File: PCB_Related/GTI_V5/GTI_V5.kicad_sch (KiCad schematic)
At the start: 165 parts, among them IC3 MAX253CSA+, IC4 AMC1306M25QDWVRQ1, IC5 AMC1306M25QDWVRQ1, IC6 AMC1306M25QDWVRQ1, IC7 MAX253CSA+, IC8 MAX253CSA+, IC9 AMC1306M25QDWVRQ1, J1 Screw_Terminal_01x03, J2 Screw_Terminal_01x02, J3 Screw_Terminal_01x02, J4 Conn_01x05_Male, J5 Conn_01x02_Male, J6 Conn_01x02_Male, K1 G5LE-1, K2 G5LE-1, Q1 BUZ11, Q2 2N7002, Q3 BUZ11, Q4 BUZ11, Q5 BUZ11, T1 760390014, T2 760390014, T3 760390014, U1 STM32L475RCTx, U2 UCC21520ADW, U3 AZ1117-5.0, U4 NCP1117-3.3_SOT223, U5 UCC21520ADW, Y1 Crystal_GND24

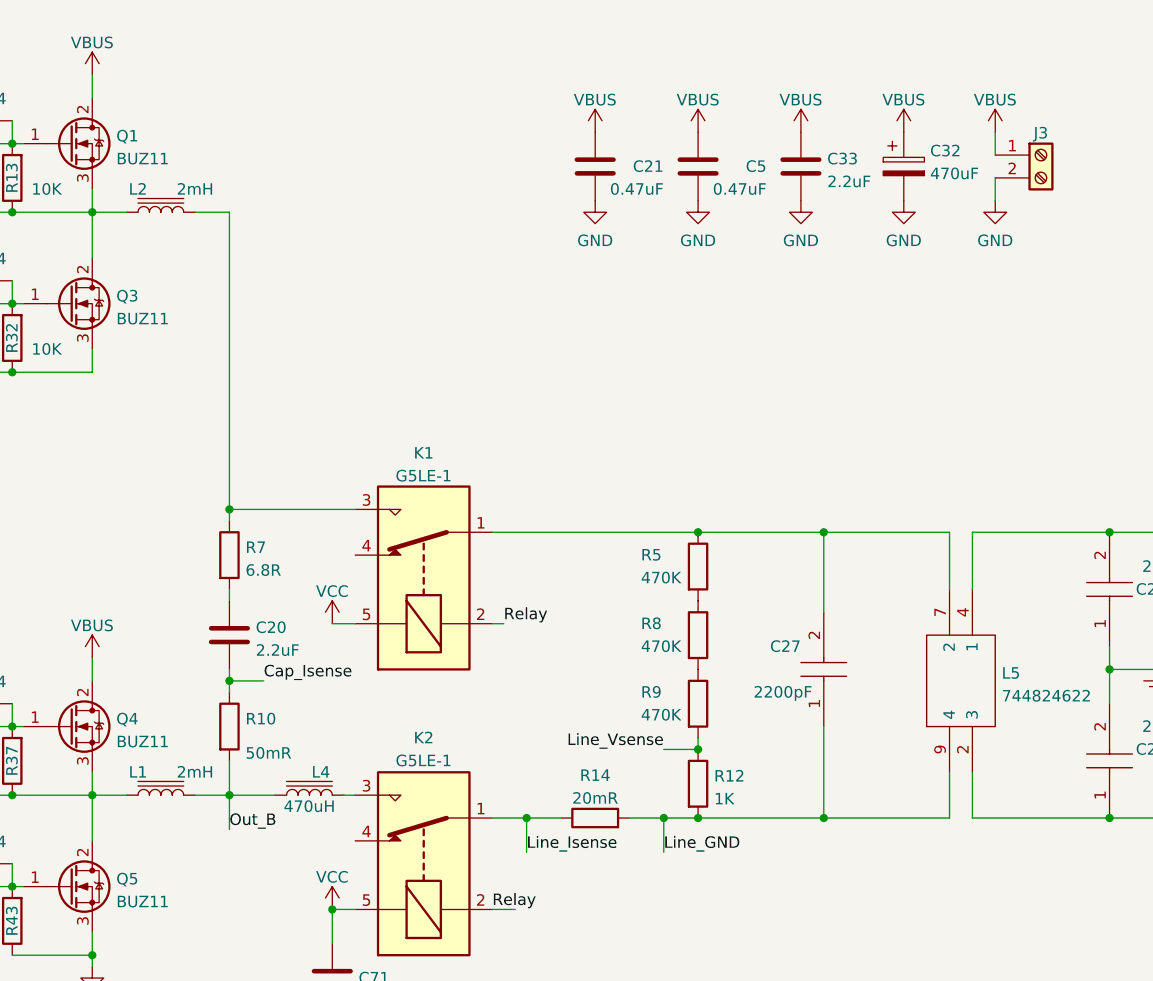
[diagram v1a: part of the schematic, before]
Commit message: updated schematic inductor values that I'm using
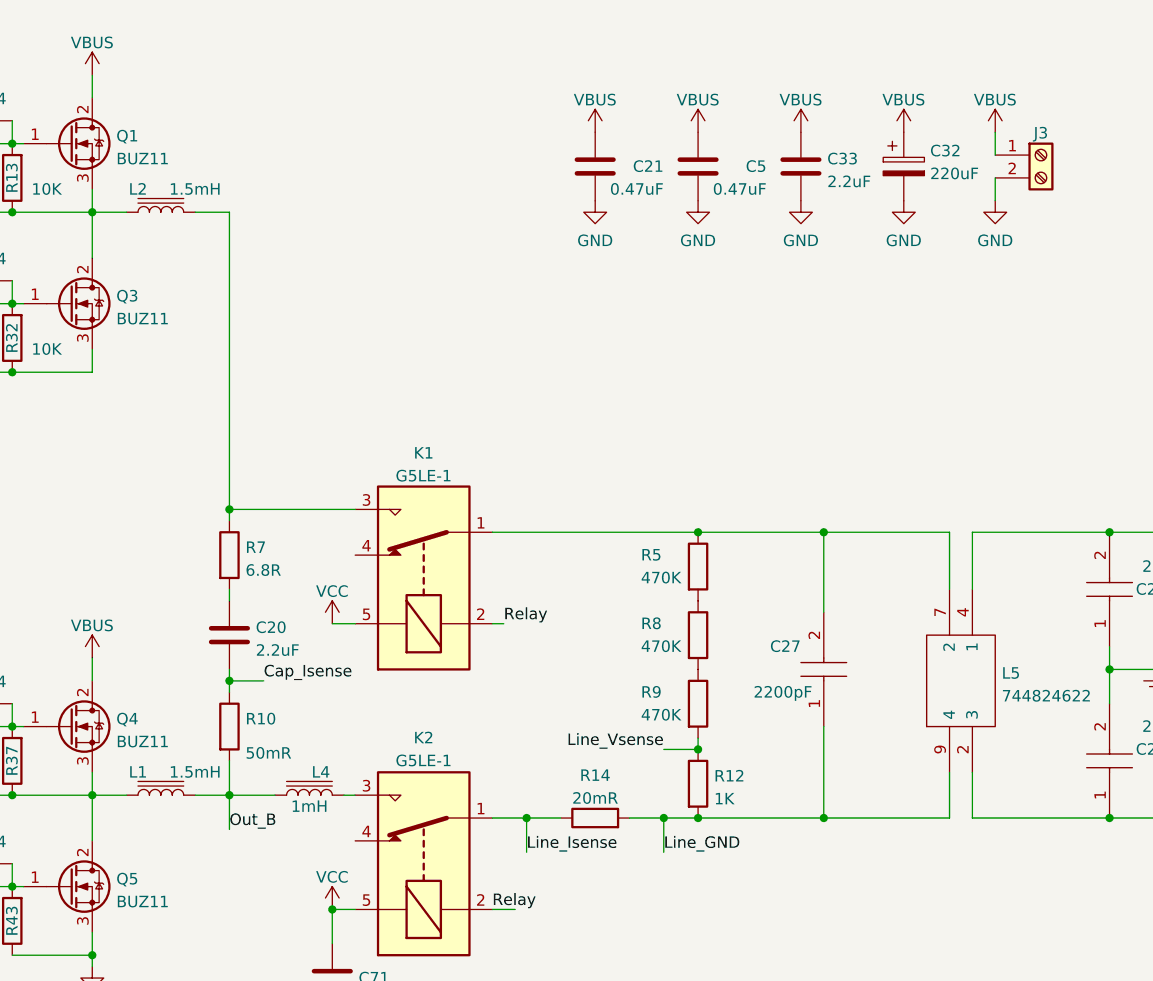
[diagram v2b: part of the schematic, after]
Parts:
- C32: value 470uF -> 220uF
- L1, L2: value 2mH -> 1.5mH
- L4: value 470uH -> 1mH
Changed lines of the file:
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@@
     (in_bom yes) (on_board yes)
     (property "Reference" "L2" (id 0) (at 276.86 46.99 90))
-    (property "Value" "2mH" (id 1) (at 283.21 46.99 90))
+    (property "Value" "1.5mH" (id 1) (at 283.21 46.99 90))
     (property "Footprint" "Inductor_THT:L_Toroid_Vertical_L35.1mm_W21.1mm_P18.50mm_Vishay_TJ6" (id 2) (at 279.4 49.53 0)
       (effects (font (size 1.27 1.27)) hide)
@@
     (in_bom yes) (on_board yes)
     (property "Reference" "L4" (id 0) (at 297.18 111.76 90))
-    (property "Value" "470uH" (id 1) (at 295.91 115.57 90))
+    (property "Value" "1mH" (id 1) (at 295.91 115.57 90))
     (property "Footprint" "Inductor_THT:L_Toroid_Vertical_L41.9mm_W19.1mm_P15.80mm_Vishay_TJ7" (id 2) (at 295.91 114.3 0)
       (effects (font (size 1.27 1.27)) hide)
@@
     (in_bom yes) (on_board yes)
     (property "Reference" "L1" (id 0) (at 276.86 111.76 90))
-    (property "Value" "2mH" (id 1) (at 283.21 111.76 90))
+    (property "Value" "1.5mH" (id 1) (at 283.21 111.76 90))
     (property "Footprint" "Inductor_THT:L_Toroid_Vertical_L35.1mm_W21.1mm_P18.50mm_Vishay_TJ6" (id 2) (at 279.4 114.3 0)
       (effects (font (size 1.27 1.27)) hide)
@@
       (effects (font (size 1.27 1.27)) (justify left))
     )
-    (property "Value" "470uF" (id 1) (at 364.871 45.2632 0)
+    (property "Value" "220uF" (id 1) (at 364.871 45.2632 0)
       (effects (font (size 1.27 1.27)) (justify left))
     )
@@
     )
     (path "/f723c92a-03f3-4352-818c-0e2a0766814e"
-      (reference "C32") (unit 1) (value "470uF") (footprint "Capacitor_THT:CP_Radial_D25.0mm_P10.00mm_SnapIn")
+      (reference "C32") (unit 1) (value "220uF") (footprint "Capacitor_THT:CP_Radial_D25.0mm_P10.00mm_SnapIn")
     )
     (path "/6ef28751-54e4-4475-8239-f1fe0de4c2f5"
@@
     )
     (path "/a87a1738-229b-4bbd-8e18-f455fecbd89e"
-      (reference "L1") (unit 1) (value "2mH") (footprint "Inductor_THT:L_Toroid_Vertical_L35.1mm_W21.1mm_P18.50mm_Vishay_TJ6")
+      (reference "L1") (unit 1) (value "1.5mH") (footprint "Inductor_THT:L_Toroid_Vertical_L35.1mm_W21.1mm_P18.50mm_Vishay_TJ6")
     )
     (path "/4796479b-7254-4ed9-8074-070c73475004"
-      (reference "L2") (unit 1) (value "2mH") (footprint "Inductor_THT:L_Toroid_Vertical_L35.1mm_W21.1mm_P18.50mm_Vishay_TJ6")
+      (reference "L2") (unit 1) (value "1.5mH") (footprint "Inductor_THT:L_Toroid_Vertical_L35.1mm_W21.1mm_P18.50mm_Vishay_TJ6")
     )
     (path "/8b129f3a-a8ef-4c29-b351-64931c69d32a"
-      (reference "L4") (unit 1) (value "470uH") (footprint "Inductor_THT:L_Toroid_Vertical_L41.9mm_W19.1mm_P15.80mm_Vishay_TJ7")
+      (reference "L4") (unit 1) (value "1mH") (footprint "Inductor_THT:L_Toroid_Vertical_L41.9mm_W19.1mm_P15.80mm_Vishay_TJ7")
     )
     (path "/0e05ca00-e93b-4516-b74e-38b8c537b248"
